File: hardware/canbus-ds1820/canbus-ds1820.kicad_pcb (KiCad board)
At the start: 4 copper layers, 55 x 35 mm, 36 parts, among them J1 USB_B_Micro, J2 SWD, J3 UART, J4 3-pole terminal, J5 CANBus, J6 CANBus, Q1 2N7002, Q2 2N7002, Q3 BSS84, U1 MCP1754S-3302xCB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

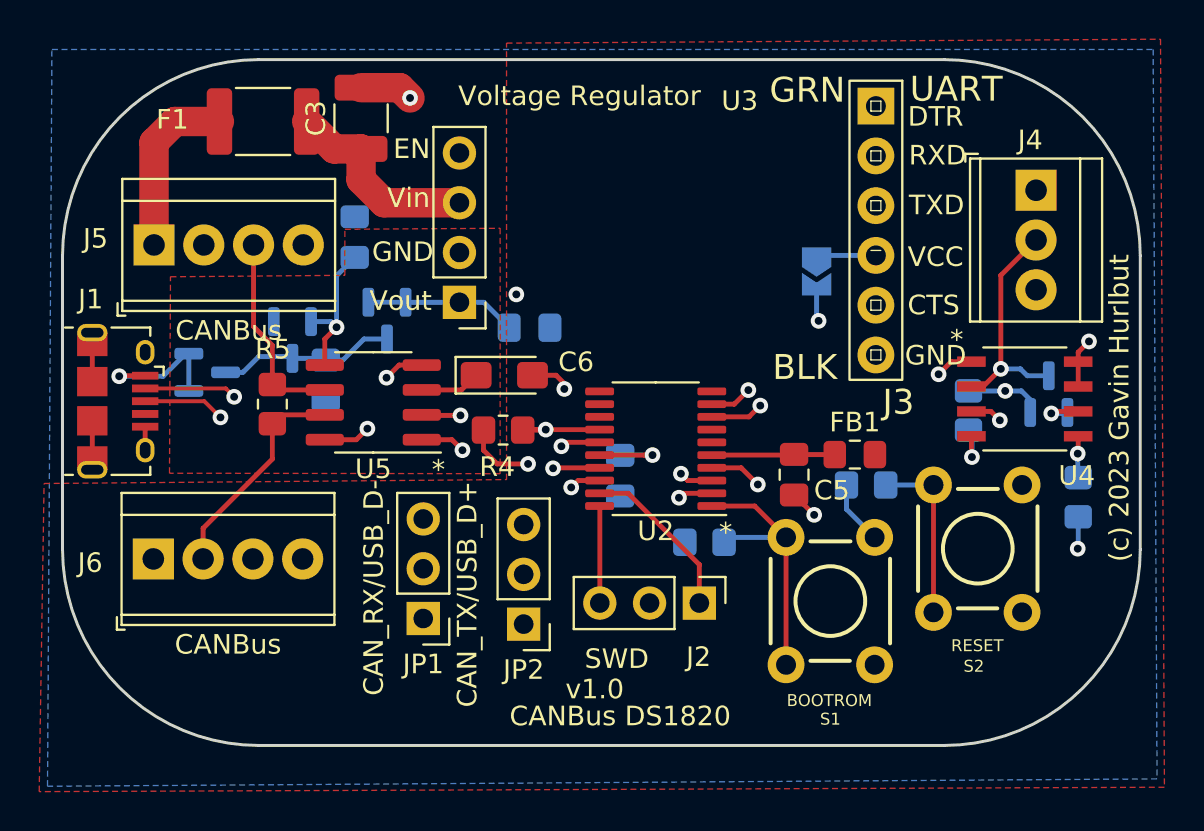
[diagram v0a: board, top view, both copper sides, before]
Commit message: Implemented DS1820 directly, no DS2482
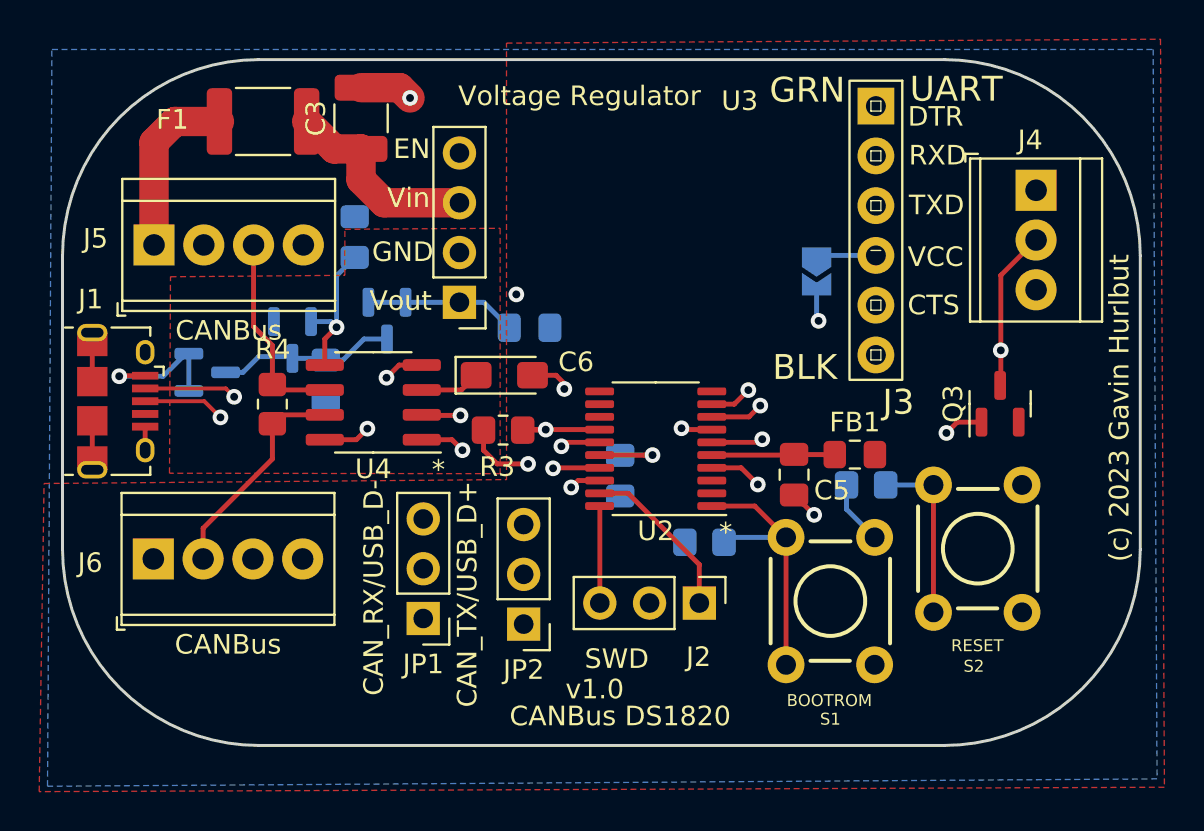
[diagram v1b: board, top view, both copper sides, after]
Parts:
- removed the R3 at (101.2, 86.5)
- removed R6: 10k, Resistor_SMD:R_0805_2012Metric_Pad1.20x1.40mm_HandSolder
- removed REF**: OSHW-Logo2_7.3x6mm_SilkScreen, Symbol:OSHW-Logo2_7.3x6mm_SilkScreen
- removed the U4 at (104.1, 85.9)
- Q3: moved to F.Cu
- moved Q3 2.53 mm to (102.8, 86.2)
- renumbered R4 to R3, R5 to R4, U5 to U4
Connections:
- U2 pad 2: SDA -> unconnected-(U2-Pad2)
- U2 pad 3: SCL -> unconnected-(U2-Pad3)
- U2 pad 6: unconnected-(U2-Pad6) -> DQ
- U2 pad 7: unconnected-(U2-Pad7) -> PCTLZ
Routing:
- net SDA: track 27.3 -> 0.00 mm, vias 2 -> 0
- net SCL: track 19.4 -> 0.00 mm, vias 2 -> 0
- net PCTLZ: track 2.27 -> 17.3 mm, vias 1 -> 2
- net DQ: track 11.8 -> 24.9 mm, vias 1 -> 2
- net +3V3: track 28.2 -> 20.6 mm, vias 8 -> 5
- net GND: track 20.6 -> 16.5 mm, vias 7 -> 5
